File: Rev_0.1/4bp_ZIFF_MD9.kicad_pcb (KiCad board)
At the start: 2 copper layers, 38.8 x 60.7 mm, 138 parts, among them CN1 MD-90SM_MD2, IC1 THS7374IPWR, IC2 TL974, J1 SMD_Conn_01x01, J2 SMD_Conn_01x01, J3 SolderJumper_3_Open, J4 SolderJumper_2_Open, J5 SMD_Conn_01x01, J6 SMD_Conn_01x01, M1PU1 SolderJumper_2_Open, P1 SMD_Conn_01x01, U1 AD725, Y1 HCM4917734475ABJT, Y2 HCM4914318180BBKT

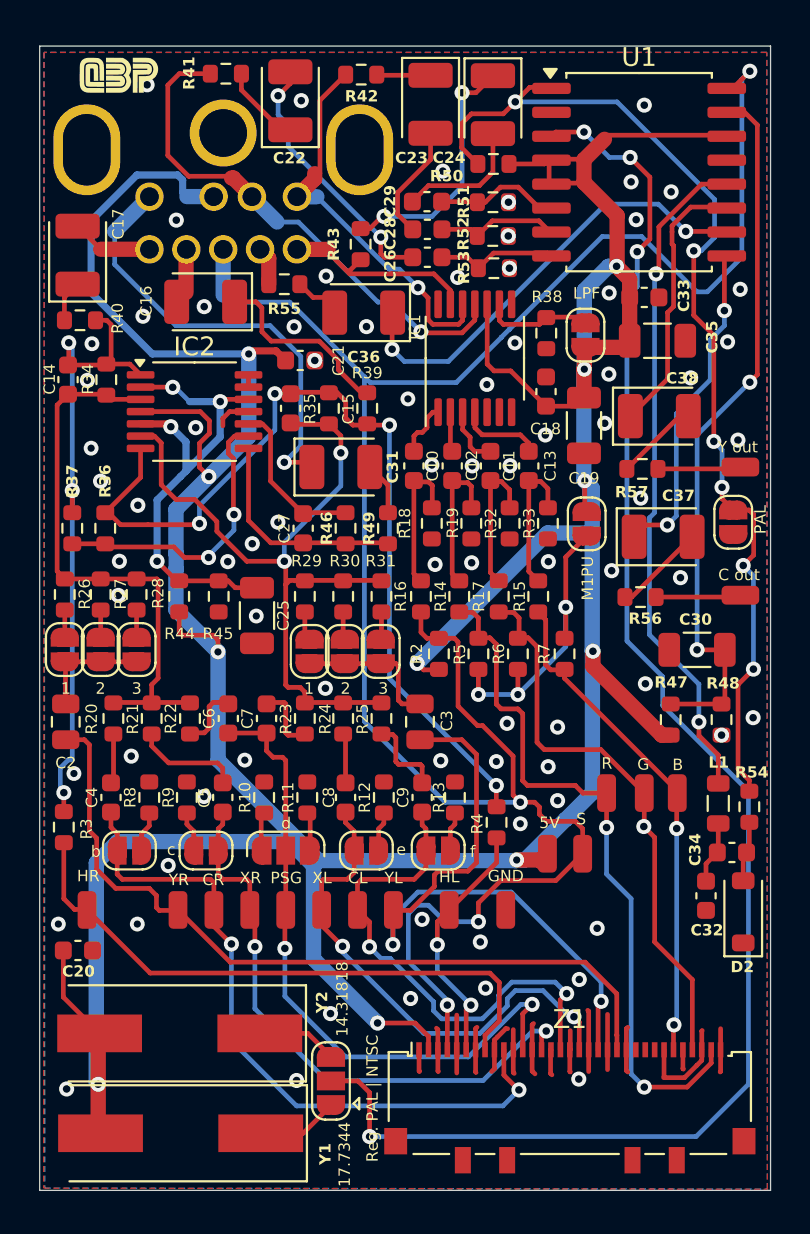
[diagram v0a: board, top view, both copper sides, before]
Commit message: Added 2nd set of jumbers for resistor isolation
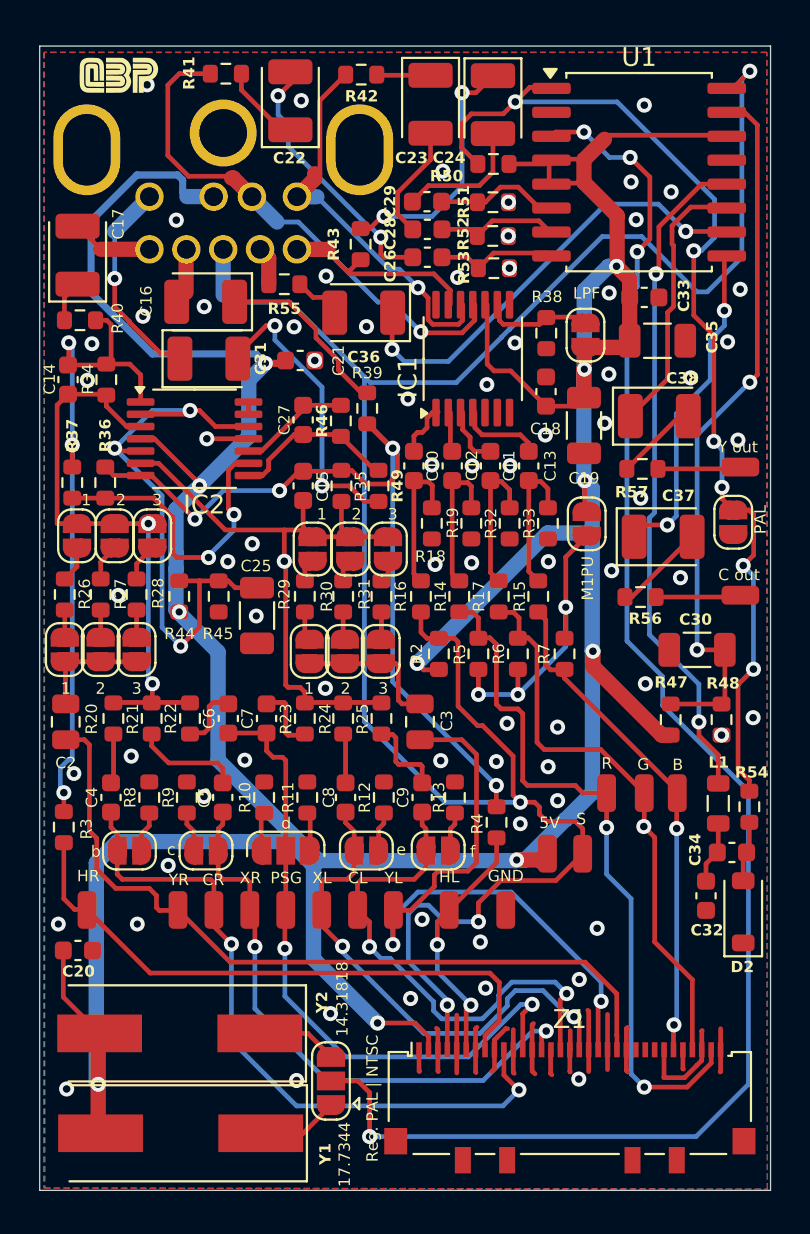
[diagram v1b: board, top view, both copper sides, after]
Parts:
- added YL5: SolderJumper_2_Open, Jumper:SolderJumper-2_P1.3mm_Open_RoundedPad1.0x1.5mm, F.Cu at (147.8, 109.8)
- added YL6: SolderJumper_2_Open, Jumper:SolderJumper-2_P1.3mm_Open_RoundedPad1.0x1.5mm, F.Cu at (149.8, 109.8)
- added YL7: SolderJumper_2_Open, Jumper:SolderJumper-2_P1.3mm_Open_RoundedPad1.0x1.5mm, F.Cu at (151.8, 109.8)
- added YR5: SolderJumper_2_Open, Jumper:SolderJumper-2_P1.3mm_Open_RoundedPad1.0x1.5mm, F.Cu at (135.3, 109.1)
- added YR6: SolderJumper_2_Open, Jumper:SolderJumper-2_P1.3mm_Open_RoundedPad1.0x1.5mm, F.Cu at (137.3, 109.1)
- added YR7: SolderJumper_2_Open, Jumper:SolderJumper-2_P1.3mm_Open_RoundedPad1.0x1.5mm, F.Cu at (139.3, 109.1)
- IC1: value THS7374IPWR -> MC33204
- IC2: value TL974 -> MC33204
- R46: value 5.5k -> 5.6k
- moved C31 9.06 mm to (142.3, 99.7)
- moved C27 5.75 mm to (147.3, 103.0)
- moved R46 5.71 mm to (149.3, 103.0)
- moved R35 4.17 mm to (149.3, 106.5)
- moved C15 4.17 mm to (147.3, 106.5)
- moved R36 2.42 mm to (135.0, 106.3)
- moved R37 2.42 mm to (136.8, 106.3)
- moved R49 2.30 mm to (151.3, 106.5), turned to -90 degrees
- moved IC2 1.44 mm to (141.5, 104.0)
- moved IC1 0.11 mm to (156.3, 99.7)
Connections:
- IC1 pad 1: Net-(IC1-CH1_IN) -> (no net)
- IC1 pad 10: +5V -> (no net)
- IC1 pad 11: B-OUT -> (no net)
- IC1 pad 12: G-OUT -> (no net)
- IC1 pad 13: R-OUT -> (no net)
- IC1 pad 14: unconnected-(IC1-CH1_OUT-Pad14) -> (no net)
- IC1 pad 2: Net-(IC1-CH2_IN) -> (no net)
- IC1 pad 3: Net-(IC1-CH3_IN) -> (no net)
- IC1 pad 4: Net-(IC1-CH4_IN) -> (no net)
- IC1 pad 5: GND -> (no net)
- IC1 pad 6: GND -> (no net)
- IC1 pad 9: Net-(IC1-BYPASS) -> (no net)
- R26 pad 2: /AUD-R -> Net-(YR5-A)
- R27 pad 2: /AUD-R -> Net-(YR6-A)
- R28 pad 2: /AUD-R -> Net-(YR7-A)
- R29 pad 2: /AUD-L -> Net-(YL5-A)
- R30 pad 2: /AUD-L -> Net-(YL6-A)
- R31 pad 2: /AUD-L -> Net-(YL7-A)
- Z1 pad MP: GND -> (no net)
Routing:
- net Net-(CN1-MONO): track 23.8 -> 11.1 mm
- net Net-(C31-Pad2): track 2.82 -> 15.5 mm, vias 0 -> 2
- net /AUD-L: track 40.9 -> 33.0 mm, vias 2 -> 1
- net +5V: track 225.3 -> 218.2 mm
- net 2V5: track 26.2 -> 32.7 mm, vias 4 -> 3
- net /OUT3: track 11.7 -> 8.87 mm
- net /OUT2: track 47.8 -> 45.2 mm
- net Net-(IC2C-+): track 8.67 -> 6.25 mm
- net Net-(YR5-A): track 0.00 -> 1.91 mm
- net /AUD-R: track 29.8 -> 31.6 mm, vias 0 -> 2
- net Net-(YR6-A): track 0.00 -> 1.72 mm
- net Net-(YR7-A): track 0.00 -> 1.53 mm
- net /OUT1: track 35.0 -> 36.4 mm
- net Net-(YL5-A): track 0.00 -> 1.28 mm
- net Net-(YL6-A): track 0.00 -> 1.20 mm
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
